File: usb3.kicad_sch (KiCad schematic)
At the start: 50 parts, among them J5 Conn_USB-C_WE_632723300011, Q19 PJE138K, Q4 PJE138K, U17 HD3SS3220RNH, U18 AP22615A_TSOT26, U19 TPD4E05U06QDQARQ1, U20 TPD4E05U06QDQARQ1, U21 TPD4E05U06QDQARQ1

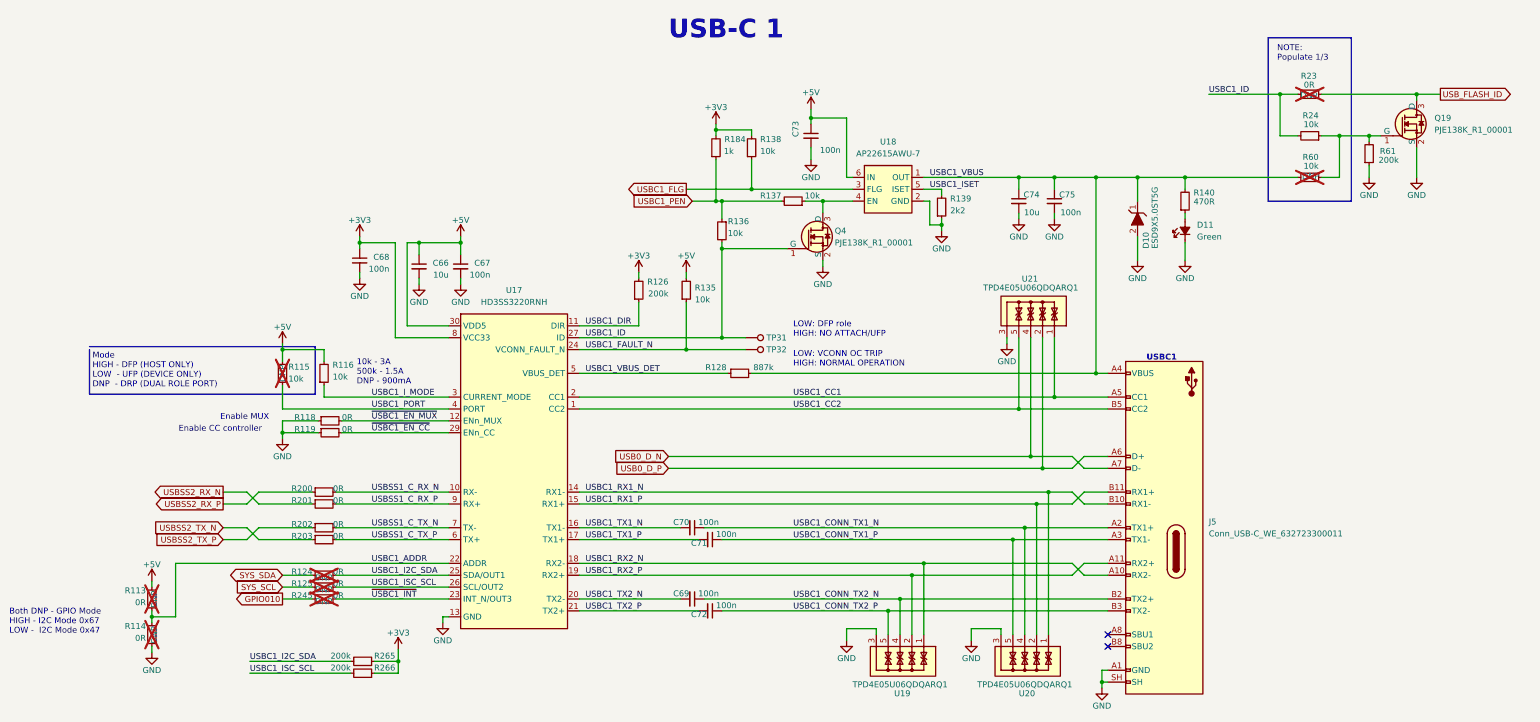
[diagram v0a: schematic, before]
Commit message: Schematic complete. Partial routing
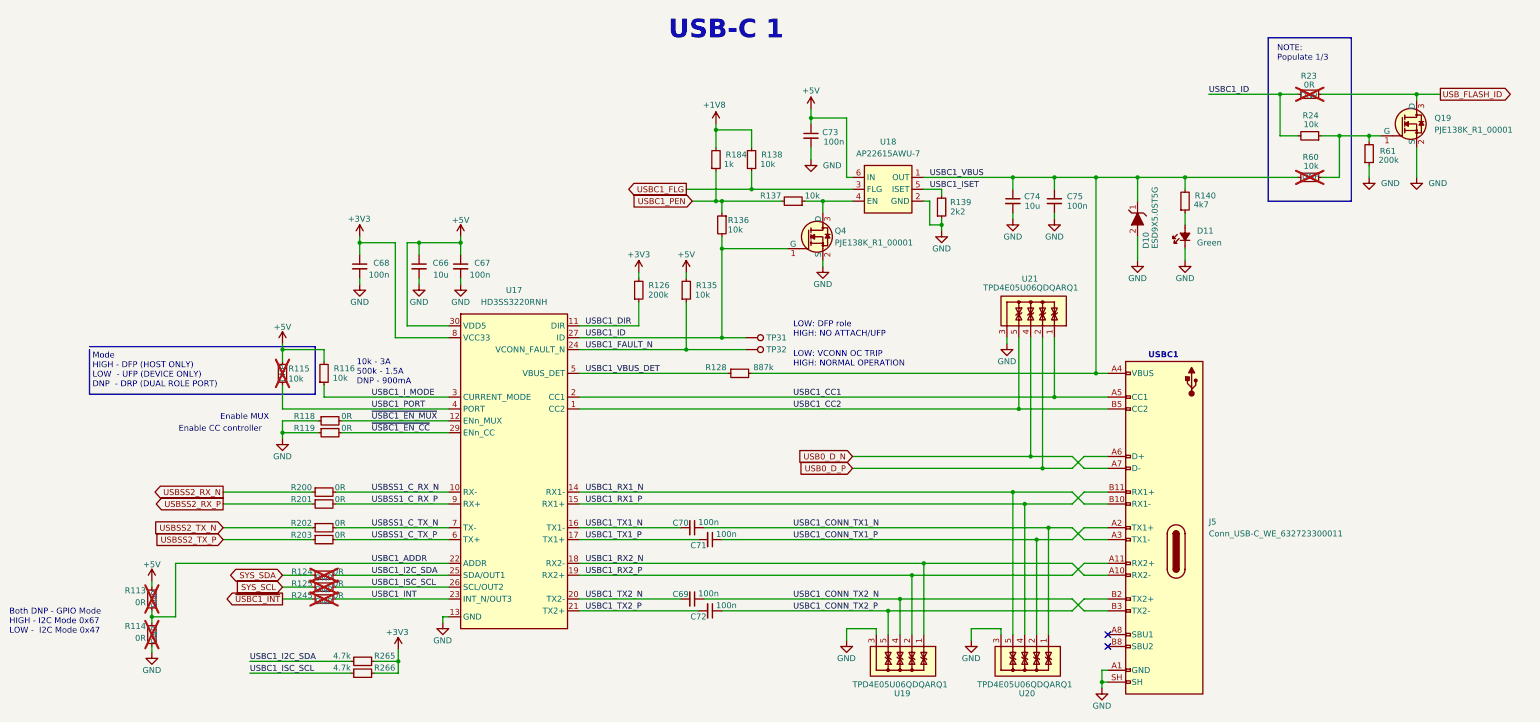
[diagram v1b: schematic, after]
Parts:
- C66: footprint antmicro-footprints:C_0603_1608Metric -> Capacitor_SMD:C_0402_1005Metric
- C67, C68: value C_100n_0402 -> C_100n_0603; footprint antmicro-footprints:C_0402_1005Metric -> Capacitor_SMD:C_0402_1005Metric
- C69, C70, C71, C72: footprint antmicro-footprints:C_0402_1005Metric -> Capacitor_SMD:C_0402_1005Metric
- C73, C75: value C_100n_0402 -> C_100n_0603; footprint antmicro-footprints:C_0402_1005Metric -> Capacitor_SMD:C_0603_1608Metric
- C74: footprint antmicro-footprints:C_0603_1608Metric -> Capacitor_SMD:C_0603_1608Metric
- D10: footprint antmicro-footprints:SOD-923 -> Diode_SMD:D_SOD-923
- D11: footprint antmicro-footprints:LED_0603_1608Metric_G -> LED_SMD:LED_0603_1608Metric
- J5: footprint antmicro-footprints:USB-C_Receptacle_WE_632723300011 -> JetsonCarrier:USB-C_Receptacle_WE_632723300011
- Q19, Q4: footprint antmicro-footprints:SOT-523 -> Package_TO_SOT_SMD:SOT-523
- R113, R114, R118, R119, R124, R125, R200, R201, R202, R203, R245: footprint antmicro-footprints:R_0402_1005Metric -> Resistor_SMD:R_0402_1005Metric
- R115, R116, R138: value R_10k_0402 -> R_10k_0603; footprint antmicro-footprints:R_0402_1005Metric -> Capacitor_SMD:C_0402_1005Metric
- R126: value R_200k_0402 -> R_200k_0603; footprint antmicro-footprints:R_0402_1005Metric -> Capacitor_SMD:C_0402_1005Metric
- R128: value R_887k_0402 -> R_887k_0603; footprint antmicro-footprints:R_0402_1005Metric -> Resistor_SMD:R_0402_1005Metric
- R135, R136, R137: value R_10k_0402 -> R_10k_0603; footprint antmicro-footprints:R_0402_1005Metric -> Resistor_SMD:R_0402_1005Metric
- R139: value R_2k2_0402 -> R_2k2_0603; footprint antmicro-footprints:R_0402_1005Metric -> Resistor_SMD:R_0402_1005Metric
- R140: value R_470R_0402 -> R_4k7_0603; footprint antmicro-footprints:R_0402_1005Metric -> Capacitor_SMD:C_0402_1005Metric; Val 470R -> 4k7
- R184: value R_1k_0402 -> R_1k_0603; footprint antmicro-footprints:R_0402_1005Metric -> Resistor_SMD:R_0402_1005Metric
- R23: value R_0R_0402 -> R_0R_0603; footprint antmicro-footprints:R_0402_1005Metric -> Resistor_SMD:R_0603_1608Metric
- R24, R60: value R_10k_0402 -> R_10k_0603; footprint antmicro-footprints:R_0402_1005Metric -> Resistor_SMD:R_0603_1608Metric
- R265, R266: value R_200k_0402 -> R_200k_0603; footprint antmicro-footprints:R_0402_1005Metric -> Resistor_SMD:R_0402_1005Metric; Val 200k -> 4.7k
- R61: value R_200k_0402 -> R_200k_0603; footprint antmicro-footprints:R_0402_1005Metric -> Resistor_SMD:R_0603_1608Metric
- TP31, TP32: footprint antmicro-footprints:TP_SMD_0.75mm -> JetsonCarrier:TP_SMD_0.75mm
- U17: footprint antmicro-footprints:WQFN-30-1EP_4.6x2.6mm_P0.4mm -> JetsonCarrier:WQFN-30-1EP_4.6x2.6mm_P0.4mm
- U18: footprint antmicro-footprints:TSOT23-6 -> Package_TO_SOT_SMD:TSOT-23-6
- U19, U20, U21: footprint antmicro-footprints:USON-10_2.5x1mm_P0.5mm -> JetsonCarrier:USON-10_2.5x1mm_P0.5mm
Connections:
- net GPIO010 is gone; now on net ~{USBC1_INT}: R245.1
- net +3V3: no longer R138.2, R184.2
- net USBC1_CONN_TX1_N: now also J5.A3 (TX1-), U20.1, U20.10; no longer J5.A2 (TX1+), U20.4, U20.7
- net USBC1_CONN_TX1_P: now also J5.A2 (TX1+), U20.2, U20.9; no longer J5.A3 (TX1-), U20.5, U20.6
- net USBC1_CONN_TX2_N: now also J5.B3 (TX2-); no longer J5.B2 (TX2+)
- net USBC1_CONN_TX2_P: now also J5.B2 (TX2+); no longer J5.B3 (TX2-)
- net USBC1_RX1_N: now also U20.5, U20.6; no longer U20.1, U20.10
- net USBC1_RX1_P: now also U20.4, U20.7; no longer U20.2, U20.9
- net USBSS2_RX_N: now also R200.1; no longer R201.1
- net USBSS2_RX_P: now also R201.1; no longer R200.1
- net USBSS2_TX_N: now also R202.1; no longer R203.1
- net USBSS2_TX_P: now also R203.1; no longer R202.1
- net ~{USBC1_INT}: no longer R245.2, U17.23 (INT_N/OUT3)
- new net +1V8: R138.2, R184.2
- new net USBC1_INT: R245.2, U17.23 (INT_N/OUT3)
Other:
- company: Antmicro Ltd -> Argus-1 Cubesat
- title: Jetson Orin Baseboard -> Jetson Carrier Board
- moved on the sheet: C68, C74, D11, R136, R138, R184
